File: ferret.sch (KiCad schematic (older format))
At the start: 41 parts

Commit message: moar progress
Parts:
- added C? (x2): 100nF, Capacitor_SMD:C_0603_1608Metric, symbol Device:C_Small
- added C?: 1uF, Capacitor_SMD:C_0603_1608Metric, symbol Device:C_Small
- added C?: 22uF, Capacitor_SMD:C_0805_2012Metric, symbol Device:C_Small
- added C?: 2.2uF, Capacitor_SMD:C_0805_2012Metric, symbol Device:C_Small
- added L?: 12uH, Inductor_SMD:L_Bourns_SRN6045TA, symbol Device:L_Core_Ferrite
- added R?: 100k, Resistor_SMD:R_0603_1608Metric, symbol Device:R_Small
- added U?: FUSB307BMPX, Package_DFN_QFN:WQFN-16-1EP_3x3mm_P0.5mm_EP1.75x1.75mm, symbol Interface_USB:FUSB307BMPX
- added U?: TPD6S300A, Package_DFN_QFN:QFN-20-1EP_3x3mm_P0.4mm_EP1.65x1.65mm, symbol meansOfCircuitDesign:TPD6S300A
- added U?: TPS560430X3F, Package_TO_SOT_SMD:SOT-23-6, symbol meansOfCircuitDesign:TPS560430X3F
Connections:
- net D+: now also J?.A6 (D+), J?.B6 (D+), U?.1 (C_SBU1); no longer U?.6 (D+)
- net D-: now also J?.A7 (D-), J?.B7 (D-), U?.2 (C_SBU2); no longer U?.7 (D-)
- net GND: now also J?.A1 (GND), J?.A12 (GND), J?.B1 (GND), J?.B12 (GND), C?.1, C?.1, C?.2, C?.2, U?.13 (GND), U?.16 (NC), U?.17 (NC), U?.18 (GND), U?.19 (D1), U?.2 (GND), U?.20 (D2), U?.21 (Thermal_Pad), U?.6 (RPD_G2), U?.7 (RPD_G1), U?.8 (GND)
- net VAC1: now also U?.6 (VBUS)
- net CC1: now reaches J?.A5 (CC1)
- net CC1: now also U?.4 (C_CC1)
- net CC2: now reaches J?.B5 (CC2)
- net CC2: now also U?.5 (C_CC2)
- net VBAT: now reaches C?.1, C?.1, J?.1 (Pin_1), R?.1, U?.22 (BAT), U?.23 (BAT)
- net VBAT: now also C?.1, U?.4 (EN), U?.5 (VIN)
- new net: U?.15 (GND), U?.17 (GND)
- new net: C?.2, U?.3 (Vbias)
- new net: C?.1, U?.1 (CB)
- new net: C?.2, L?.1, U?.6 (SW)
- new net +3V3: C?.1, C?.2, L?.2, R?.1, U?.10 (Vpwr), U?.3 (FB), U?.5 (LDO), U?.7 (VDD)
- new net CC1_PROT: U?.1 (CC1), U?.12 (CC1)
- new net CC2_PROT: U?.11 (CC2), U?.3 (CC2)
- new net D_PROT+: U?.15 (SBU1), U?.6 (D+)
- new net D_PROT-: U?.14 (SBU2), U?.7 (D-)
- new net ~FAULT: R?.2, U?.16 (GPIO1), U?.9 (~FAULT)

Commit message: almost there
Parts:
- added C? (x2): 1uF, Capacitor_SMD:C_0603_1608Metric, symbol Device:C_Small
- added C?: 100nF, Capacitor_SMD:C_0603_1608Metric, symbol Device:C_Small
- added D?: 10V, symbol Device:D_Schottky_Small
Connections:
- net +3V3: now also C?.2, D?.1 (K); no longer U?.5 (LDO)
- net GND: now also U?.15 (GND), U?.17 (GND), C?.1, C?.2, C?.2
- net VAC1: now also C?.1
- new net: C?.1, D?.2 (A), U?.5 (LDO)
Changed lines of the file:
@@
 U 1 1 5EF017EC
 P 5350 6550
-F 0 "U?" H 5350 5861 50  0000 C CNN
-F 1 "FUSB307BMPX" H 5350 5770 50  0000 C CNN
+F 0 "U?" H 5900 6000 50  0000 C CNN
+F 1 "FUSB307BMPX" H 5000 6000 50  0000 C CNN
 F 2 "Package_DFN_QFN:WQFN-16-1EP_3x3mm_P0.5mm_EP1.75x1.75mm" H 5350 5850 50  0001 C CNN
 F 3 "http://www.onsemi.com/pub/Collateral/FUSB307B-D.PDF" H 5350 5950 50  0001 C CNN
@@
 Wire Wire Line
 	2150 5500 2150 5450
-$Comp
-L power:+3V3 #PWR?
-U 1 1 5F12DE2D
-P 5150 5700
-F 0 "#PWR?" H 5150 5550 50  0001 C CNN
-F 1 "+3V3" H 5165 5873 50  0000 C CNN
-F 2 "" H 5150 5700 50  0001 C CNN
-F 3 "" H 5150 5700 50  0001 C CNN
-	1    5150 5700
-	1    0    0    -1
-$EndComp
-Wire Wire Line
-	5150 5700 5150 5950
+Wire Wire Line
+	5150 5450 5150 5800
 Wire Wire Line
 	2850 2600 2850 2850
@@
 Wire Wire Line
 	6350 6850 6050 6850
-Text Label 5250 5700 3    50   ~ 0
+Text Label 5250 5250 3    50   ~ 0
 VAC1
 Wire Wire Line
-	5250 5700 5250 5950
+	5250 5250 5250 5450
 $Comp
 L meansOfCircuitDesign:TPS560430X3F U?
@@
 $EndComp
 Wire Wire Line
-	5450 5950 5450 5700
+	5450 5950 5450 5800
 Wire Wire Line
 	4600 4600 5300 4600
@@
 Wire Wire Line
 	8950 2350 9350 2350
+$Comp
+L Device:C_Small C?
+U 1 1 5F2FDC42
+P 5650 5450
+F 0 "C?" V 5879 5450 50  0000 C CNN
+F 1 "1uF" V 5788 5450 50  0000 C CNN
+F 2 "Capacitor_SMD:C_0603_1608Metric" H 5650 5450 50  0001 C CNN
+F 3 "~" H 5650 5450 50  0001 C CNN
+	1    5650 5450
+	0    -1   -1   0
+$EndComp
+$Comp
+L Device:C_Small C?
+U 1 1 5F31ED13
+P 5650 5800
+F 0 "C?" V 5421 5800 50  0000 C CNN
+F 1 "100nF" V 5512 5800 50  0000 C CNN
+F 2 "Capacitor_SMD:C_0603_1608Metric" H 5650 5800 50  0001 C CNN
+F 3 "~" H 5650 5800 50  0001 C CNN
+	1    5650 5800
+	0    1    1    0
+$EndComp
+Wire Wire Line
+	5550 5800 5450 5800
+Connection ~ 5450 5800
+Wire Wire Line
+	5450 5800 5450 5700
+$Comp
+L power:GND #PWR?
+U 1 1 5F3427A4
+P 5800 5850
+F 0 "#PWR?" H 5800 5600 50  0001 C CNN
+F 1 "GND" H 5888 5813 50  0000 L CNN
+F 2 "" H 5800 5850 50  0001 C CNN
+F 3 "" H 5800 5850 50  0001 C CNN
+	1    5800 5850
+	1    0    0    -1
+$EndComp
+Wire Wire Line
+	5800 5850 5800 5800
+Wire Wire Line
+	5800 5800 5750 5800
+Wire Wire Line
+	5550 5450 5250 5450
+Connection ~ 5250 5450
+Wire Wire Line
+	5250 5450 5250 5950
+Wire Wire Line
+	5750 5450 5800 5450
+Wire Wire Line
+	5800 5450 5800 5800
+Connection ~ 5800 5800
+$Comp
+L power:GND #PWR?
+U 1 1 5F39A504
+P 5350 7200
+F 0 "#PWR?" H 5350 6950 50  0001 C CNN
+F 1 "GND" H 5355 7027 50  0000 C CNN
+F 2 "" H 5350 7200 50  0001 C CNN
+F 3 "" H 5350 7200 50  0001 C CNN
+	1    5350 7200
+	1    0    0    -1
+$EndComp
+Wire Wire Line
+	5350 7200 5350 7150
+Connection ~ 5150 5800
+Wire Wire Line
+	5150 5800 5150 5950
+Wire Wire Line
+	4750 5800 4850 5800
+Wire Wire Line
+	4750 5850 4750 5800
+$Comp
+L power:GND #PWR?
+U 1 1 5F3F5C10
+P 4750 5850
+F 0 "#PWR?" H 4750 5600 50  0001 C CNN
+F 1 "GND" H 4600 5800 50  0000 C CNN
+F 2 "" H 4750 5850 50  0001 C CNN
+F 3 "" H 4750 5850 50  0001 C CNN
+	1    4750 5850
+	1    0    0    -1
+$EndComp
+Wire Wire Line
+	5050 5800 5150 5800
+Wire Wire Line
+	4750 5450 4850 5450
+Wire Wire Line
+	4750 5350 4750 5450
+Wire Wire Line
+	5150 5450 5050 5450
+$Comp
+L Device:D_Schottky_Small D?
+U 1 1 5F3BF43E
+P 4950 5450
+F 0 "D?" H 4950 5657 50  0000 C CNN
+F 1 "10V" H 4950 5566 50  0000 C CNN
+F 2 "" V 4950 5450 50  0001 C CNN
+F 3 "~" V 4950 5450 50  0001 C CNN
+	1    4950 5450
+	1    0    0    -1
+$EndComp
+$Comp
+L Device:C_Small C?
+U 1 1 5F3AC993
+P 4950 5800
+F 0 "C?" V 4721 5800 50  0000 C CNN
+F 1 "1uF" V 4812 5800 50  0000 C CNN
+F 2 "Capacitor_SMD:C_0603_1608Metric" H 4950 5800 50  0001 C CNN
+F 3 "~" H 4950 5800 50  0001 C CNN
+	1    4950 5800
+	0    1    1    0
+$EndComp
+$Comp
+L power:+3V3 #PWR?
+U 1 1 5F12DE2D
+P 4750 5350
+F 0 "#PWR?" H 4750 5200 50  0001 C CNN
+F 1 "+3V3" H 4765 5523 50  0000 C CNN
+F 2 "" H 4750 5350 50  0001 C CNN
+F 3 "" H 4750 5350 50  0001 C CNN
+	1    4750 5350
+	1    0    0    -1
+$EndComp
 $EndSCHEMATC

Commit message: more changes
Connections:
- net GND: now also J?.S1 (SHIELD)
- no-connect marks 10 -> 13
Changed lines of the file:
@@
 	1    0    0    -1
 $EndComp
+NoConn ~ 4650 6350
+NoConn ~ 4650 6450
+NoConn ~ 5350 5950
+$Comp
+L power:GND #PWR?
+U 1 1 5F5FECEC
+P 1850 5500
+F 0 "#PWR?" H 1850 5250 50  0001 C CNN
+F 1 "GND" H 1855 5327 50  0000 C CNN
+F 2 "" H 1850 5500 50  0001 C CNN
+F 3 "" H 1850 5500 50  0001 C CNN
+	1    1850 5500
+	1    0    0    -1
+$EndComp
+Wire Wire Line
+	1850 5500 1850 5450
 $EndSCHEMATC

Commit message: Schematic is pretty much finished now
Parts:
- added R? (x4): 10k, Resistor_SMD:R_0603_1608Metric, symbol Device:R_Small
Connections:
- net +3V3: now also U?.12 (~QON), R?.1, R?.2, R?.2
- net GND: now also U?.8 (DBG_N), R?.1
- net ~CE: now reaches U?.13 (~CE)
- net ~CE: now also R?.2
- net SCL: now reaches U?.14 (SCL)
- net SCL: now also U?.11 (SCL1/SDA2)
- net SDA: now reaches U?.15 (SDA)
- net SDA: now also U?.12 (SDA1/SCL2)
- net ~INT_CHG: now reaches U?.21 (~INT)
- net ~INT_PMC: now reaches U?.10 (INT_N)
- net ~INT_PMC: now also R?.1
- net at U?.4 (ORIENT/I2C_ADDR): now also R?.1, R?.2
- no-connect marks 13 -> 14
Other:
- moved on the sheet: C?, D?, J?, L?, Q?, R?, U?

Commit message: some shuffeling
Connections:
- net ~FAULT renamed ~PROT_FLT
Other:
- moved on the sheet: C?, D?, J?, L?, Q?, R?, U?

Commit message: Annotate schematic
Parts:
- removed D?: 12V, symbol Device:D_Schottky_Small
- added D3: 12V, symbol Device:D_Zener_Small
- D1: renamed from D?; symbol Device:D_Schottky_Small -> Device:D_Zener_Small
- gave numbers to parts that had none: 57
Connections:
- net ACDRV2: now also D3.1 (K)
- net VBAT: no longer C14.1, U4.4 (EN), U4.5 (VIN)
- net VCC: now also C14.1, U4.4 (EN), U4.5 (VIN)
- net at C7.2, Q3.1 (S), Q4.1 (S): now also D3.2 (A)

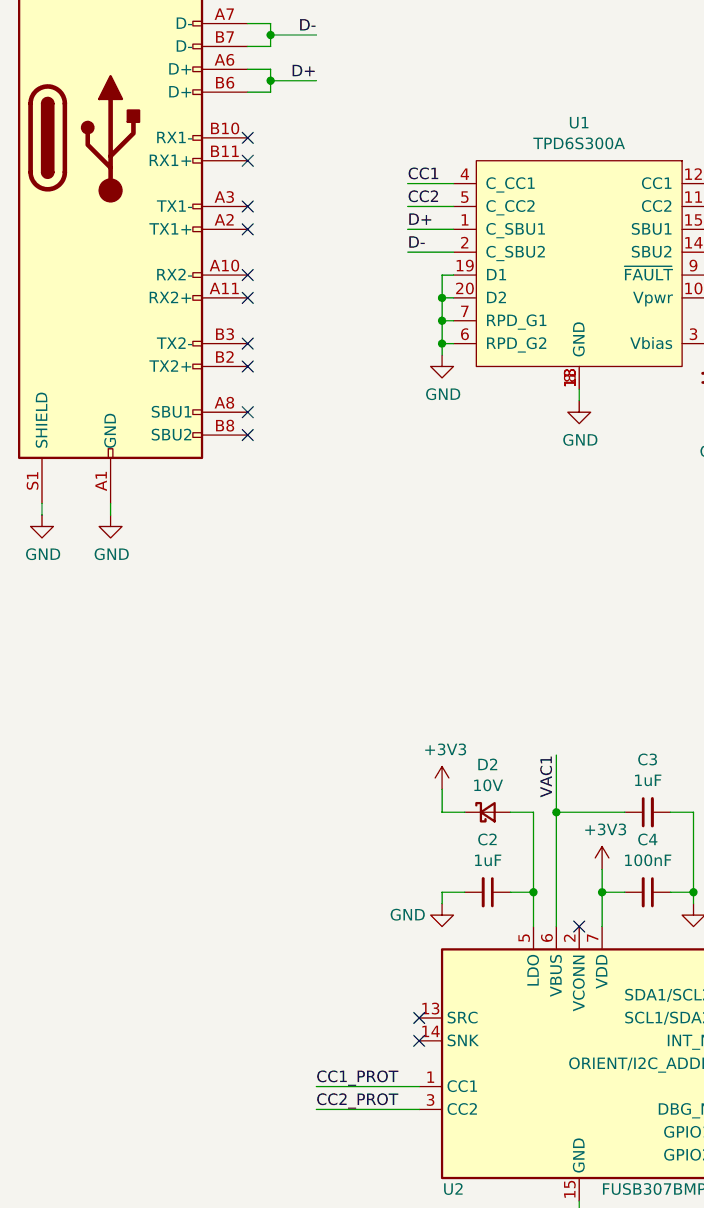
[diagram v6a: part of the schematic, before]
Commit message: Enable dead battery operation
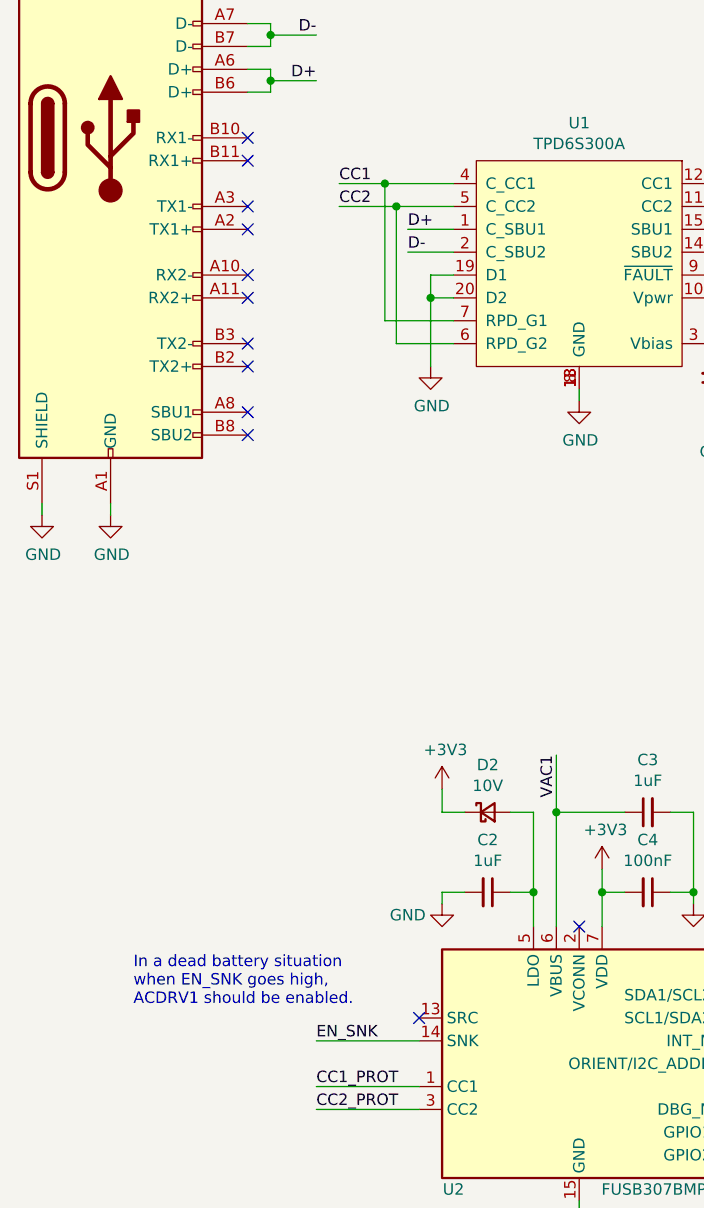
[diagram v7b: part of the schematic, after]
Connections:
- net CC1: now also U1.7 (RPD_G1)
- net CC2: now also U1.6 (RPD_G2)
- net GND: no longer U1.6 (RPD_G2), U1.7 (RPD_G1)
- net EN_SNK: now reaches U2.14 (SNK)
- no-connect marks 14 -> 13
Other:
- note added: "In a dead battery situation\nwhen EN_SNK goes high,\nACDRV1 should be enabled."
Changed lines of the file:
@@
 	1850 1900 2050 1900
 Wire Wire Line
-	2750 2900 2550 2900
-Wire Wire Line
-	2550 2800 2750 2800
-Text Label 2550 2900 0    50   ~ 0
+	2750 2900 2500 2900
+Wire Wire Line
+	2250 2800 2450 2800
+Text Label 2250 2900 0    50   ~ 0
 CC2
-Text Label 2550 2800 0    50   ~ 0
+Text Label 2250 2800 0    50   ~ 0
 CC1
 $Comp
@@
 L power:GND #PWR03
 U 1 1 5F008D24
-P 2700 3550
-F 0 "#PWR03" H 2700 3300 50  0001 C CNN
-F 1 "GND" H 2705 3377 50  0000 C CNN
-F 2 "" H 2700 3550 50  0001 C CNN
-F 3 "" H 2700 3550 50  0001 C CNN
-	1    2700 3550
-	1    0    0    -1
-$EndComp
-Wire Wire Line
-	2700 3550 2700 3500
-Wire Wire Line
-	2700 3400 2750 3400
-Wire Wire Line
-	2750 3500 2700 3500
-Connection ~ 2700 3500
-Wire Wire Line
-	2700 3500 2700 3400
+P 2650 3600
+F 0 "#PWR03" H 2650 3350 50  0001 C CNN
+F 1 "GND" H 2655 3427 50  0000 C CNN
+F 2 "" H 2650 3600 50  0001 C CNN
+F 3 "" H 2650 3600 50  0001 C CNN
+	1    2650 3600
+	1    0    0    -1
+$EndComp
 $Comp
 L Device:C_Small C5
@@
 ~PROT_FLT
 Wire Wire Line
-	2750 3200 2700 3200
-Wire Wire Line
-	2700 3200 2700 3300
-Connection ~ 2700 3400
-Wire Wire Line
-	2750 3300 2700 3300
-Connection ~ 2700 3300
-Wire Wire Line
-	2700 3300 2700 3400
+	2750 3200 2650 3200
+Wire Wire Line
+	2650 3200 2650 3300
+Wire Wire Line
+	2750 3300 2650 3300
 $Comp
 L power:GND #PWR02
@@
 $EndComp
 NoConn ~ 3300 6050
-NoConn ~ 2600 6550
 NoConn ~ 2600 6450
 $Comp
@@
 	7650 5800 7650 5850
 Connection ~ 7650 5850
+Wire Wire Line
+	2750 3400 2450 3400
+Wire Wire Line
+	2450 3400 2450 2800
+Connection ~ 2450 2800
+Wire Wire Line
+	2450 2800 2750 2800
+Wire Wire Line
+	2500 2900 2500 3500
+Wire Wire Line
+	2500 3500 2750 3500
+Connection ~ 2500 2900
+Wire Wire Line
+	2500 2900 2250 2900
+Wire Wire Line
+	2650 3300 2650 3600
+Connection ~ 2650 3300
+Text Label 2150 6550 0    50   ~ 0
+EN_SNK
+Wire Wire Line
+	2150 6550 2600 6550
+Text Notes 1350 6400 0    50   ~ 0
+In a dead battery situation\nwhen EN_SNK goes high,\nACDRV1 should be enabled.
 $EndSCHEMATC

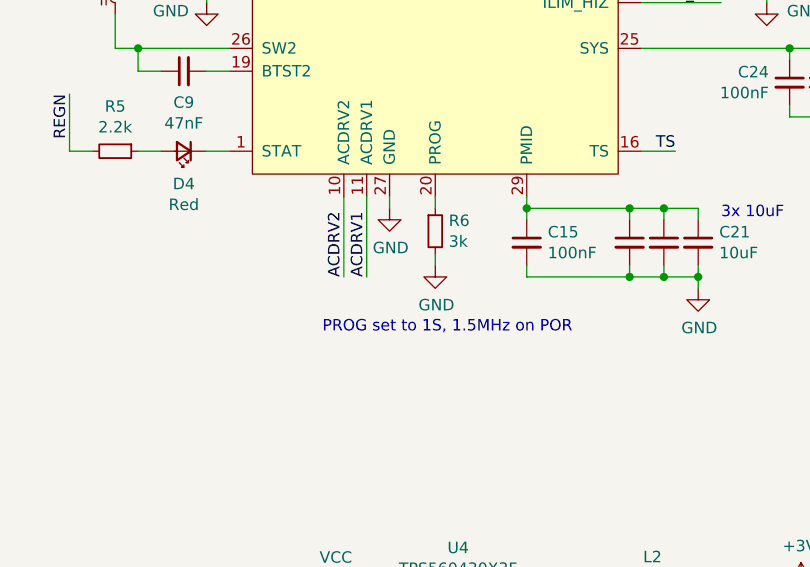
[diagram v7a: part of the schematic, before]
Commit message: Set to 2S default so that VSYS will always be higher than 4V
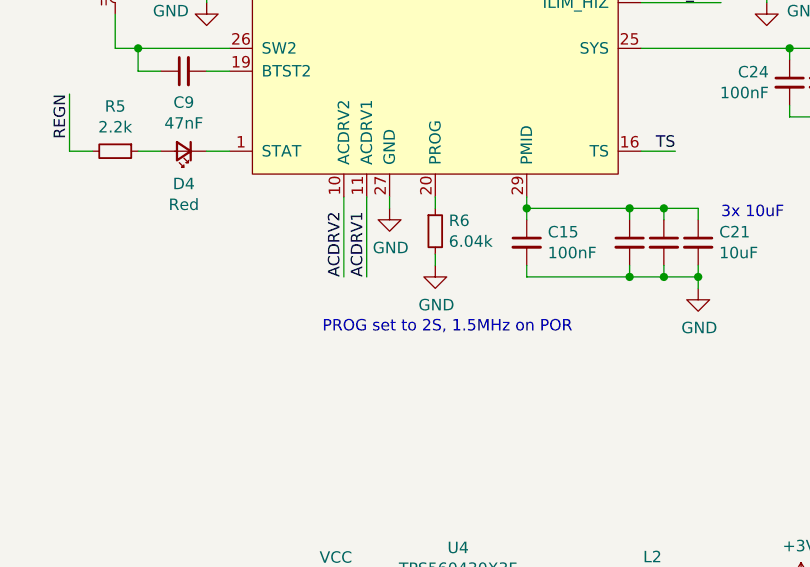
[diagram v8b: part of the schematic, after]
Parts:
- R6: value 3k -> 6.04k
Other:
- note added: "PROG set to 2S, 1.5MHz on POR"
- note removed: "PROG set to 1S, 1.5MHz on POR"
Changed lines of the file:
@@
 P 8100 4200
 F 0 "R6" H 8159 4246 50  0000 L CNN
-F 1 "3k" H 8159 4155 50  0000 L CNN
+F 1 "6.04k" H 8159 4155 50  0000 L CNN
 F 2 "Resistor_SMD:R_0603_1608Metric" H 8100 4200 50  0001 C CNN
 F 3 "~" H 8100 4200 50  0001 C CNN
@@
 	8100 4350 8100 4300
 Text Notes 8700 4650 2    50   ~ 0
-PROG set to 1S, 1.5MHz on POR
+PROG set to 2S, 1.5MHz on POR
 $Comp
 L power:GND #PWR030
